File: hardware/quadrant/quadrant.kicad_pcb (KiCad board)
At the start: 4 copper layers, 220 x 200 mm, 347 parts, among them J1 FPC 16, P1 NPTH, Q1 AO3401A, Q111 AO3400A, Q112 AO3401A, Q121 AO3400A, Q122 AO3401A, Q131 AO3400A, Q132 AO3401A, Q141 AO3400A, Q142 AO3401A, Q151 AO3400A, Q152 AO3401A, Q161 AO3400A, Q162 AO3401A, Q171 AO3400A, Q172 AO3401A, Q181 AO3400A, Q182 AO3401A, Q191 AO3400A, Q192 AO3401A, Q2 AO3400A, Q201 AO3400A, Q202 AO3401A, Q211 AO3400A, Q212 AO3401A, Q221 AO3400A, Q222 AO3401A, Q231 AO3400A, Q232 AO3401A, Q241 AO3400A, Q242 AO3401A, Q251 AO3400A, Q252 AO3401A, Q261 AO3400A, Q262 AO3401A, U1 74HC4514, U2 74HC154, U3 ADG1607, U4 ADG1607, U5 AD8421, U6 74LVC1G04, U7 OPA2810, U8 OPA2810

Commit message: Quadrant : build final avec les éventails tenus hors du bord
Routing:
- net M8_B: track 2.21 -> 0.71 mm, vias 1 -> 0
- net M6_B: track 2.21 -> 0.71 mm, vias 1 -> 0
- net M4_B: track 2.21 -> 0.71 mm, vias 1 -> 0
- net M2_B: track 2.21 -> 0.71 mm, vias 1 -> 0
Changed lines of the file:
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@@
   (via (at 14.7 98.65) (size 0.45) (drill 0.2) (layers "F.Cu" "B.Cu") (net 37))
   (segment (start 2.9625 110.075) (end 2.25 110.075) (width 0.2) (layer "F.Cu") (net 117))
-  (segment (start 2.25 110.075) (end 0.75 110.075) (width 0.2) (layer "F.Cu") (net 117))
-  (via (at 0.75 110.075) (size 0.45) (drill 0.2) (layers "F.Cu" "B.Cu") (net 117))
   (segment (start 2.9625 110.575) (end 2.25 110.575) (width 0.2) (layer "F.Cu") (net 112))
   (segment (start 2.25 110.575) (end 1.45 110.575) (width 0.2) (layer "F.Cu") (net 112))
   (via (at 1.45 110.575) (size 0.45) (drill 0.2) (layers "F.Cu" "B.Cu") (net 112))
   (segment (start 2.9625 111.075) (end 2.25 111.075) (width 0.2) (layer "F.Cu") (net 107))
-  (segment (start 2.25 111.075) (end 0.75 111.075) (width 0.2) (layer "F.Cu") (net 107))
-  (via (at 0.75 111.075) (size 0.45) (drill 0.2) (layers "F.Cu" "B.Cu") (net 107))
   (segment (start 2.9625 111.575) (end 2.25 111.575) (width 0.2) (layer "F.Cu") (net 102))
   (segment (start 2.25 111.575) (end 1.45 111.575) (width 0.2) (layer "F.Cu") (net 102))
   (via (at 1.45 111.575) (size 0.45) (drill 0.2) (layers "F.Cu" "B.Cu") (net 102))
   (segment (start 2.9625 112.075) (end 2.25 112.075) (width 0.2) (layer "F.Cu") (net 97))
-  (segment (start 2.25 112.075) (end 0.75 112.075) (width 0.2) (layer "F.Cu") (net 97))
-  (via (at 0.75 112.075) (size 0.45) (drill 0.2) (layers "F.Cu" "B.Cu") (net 97))
   (segment (start 2.9625 112.575) (end 2.25 112.575) (width 0.2) (layer "F.Cu") (net 92))
   (segment (start 2.25 112.575) (end 1.45 112.575) (width 0.2) (layer "F.Cu") (net 92))
   (via (at 1.45 112.575) (size 0.45) (drill 0.2) (layers "F.Cu" "B.Cu") (net 92))
   (segment (start 2.9625 113.075) (end 2.25 113.075) (width 0.2) (layer "F.Cu") (net 87))
-  (segment (start 2.25 113.075) (end 0.75 113.075) (width 0.2) (layer "F.Cu") (net 87))
-  (via (at 0.75 113.075) (size 0.45) (drill 0.2) (layers "F.Cu" "B.Cu") (net 87))
   (segment (start 2.9625 113.575) (end 2.25 113.575) (width 0.2) (layer "F.Cu") (net 82))
   (segment (start 2.25 113.575) (end 1.45 113.575) (width 0.2) (layer "F.Cu") (net 82))

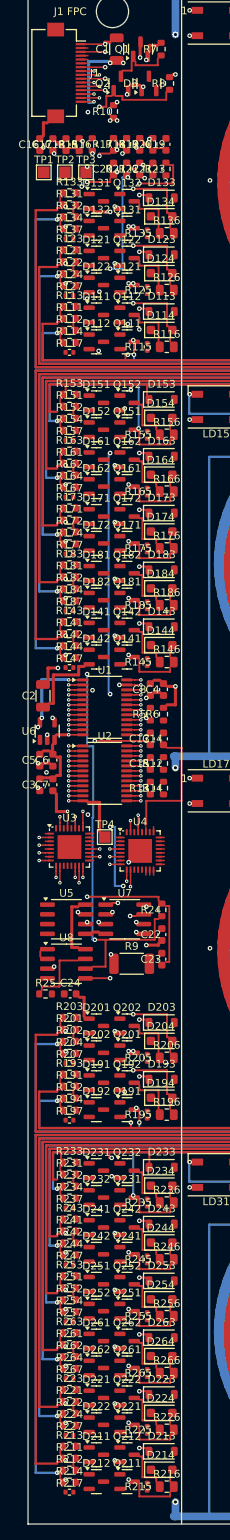
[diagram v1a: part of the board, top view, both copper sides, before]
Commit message: Quadrant 4 x 4 régénéré : schéma dessiné à huit feuilles, roue libre, BAV99W, résultats de build et de DRC
hardware/quadrant : feuille racine et feuilles rails, cells-1 à
cells-4, select, chain, leds ; PCB reroutée avec le nouveau plan de
cellule. Build : aucune route LED ou alimentation ouverte, aucun défaut
d'isolement, neuf nets du frontal à finir dans pcbnew (VREF route
désormais) ; DRC KiCad sans erreur hors éléments non connectés. README
du quadrant et tableau de résultats de la note 14 à jour, avec la ligne
du quadrant 2 x 2.
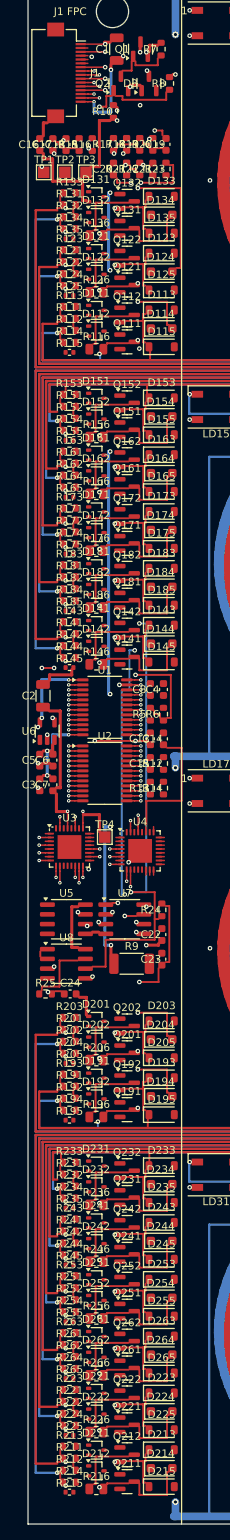
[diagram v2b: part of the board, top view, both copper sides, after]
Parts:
- removed R117, R127, R137, R147, R157, R167, R177, R187, R197, R207, R217, R227, R237, R247, R257, R267: 100k, Resistor_SMD:R_0402_1005Metric
- added D115: B5819W, Diode_SMD:D_SOD-123, F.Cu at (17.4, 46.7)
- added D125: B5819W, Diode_SMD:D_SOD-123, F.Cu at (17.4, 39.3)
- added D135: B5819W, Diode_SMD:D_SOD-123, F.Cu at (17.4, 31.9)
- added D145: B5819W, Diode_SMD:D_SOD-123, F.Cu at (17.4, 87.7)
- added D155: B5819W, Diode_SMD:D_SOD-123, F.Cu at (17.4, 58.1)
- added D165: B5819W, Diode_SMD:D_SOD-123, F.Cu at (17.4, 65.5)
- added D175: B5819W, Diode_SMD:D_SOD-123, F.Cu at (17.4, 72.9)
- added D185: B5819W, Diode_SMD:D_SOD-123, F.Cu at (17.4, 80.3)
- added D195: B5819W, Diode_SMD:D_SOD-123, F.Cu at (17.4, 146.7)
- added D205: B5819W, Diode_SMD:D_SOD-123, F.Cu at (17.4, 139.3)
- added D215: B5819W, Diode_SMD:D_SOD-123, F.Cu at (17.4, 195.1)
- added D225: B5819W, Diode_SMD:D_SOD-123, F.Cu at (17.4, 187.7)
- added D235: B5819W, Diode_SMD:D_SOD-123, F.Cu at (17.4, 158.1)
- added D245: B5819W, Diode_SMD:D_SOD-123, F.Cu at (17.4, 165.5)
- added D255: B5819W, Diode_SMD:D_SOD-123, F.Cu at (17.4, 172.9)
- added D265: B5819W, Diode_SMD:D_SOD-123, F.Cu at (17.4, 180.3)
- D111, D112, D121, D122, D131, D132, D141, D142, D151, D152, D161, D162, D171, D172, D181, D182, D191, D192, D201, D202, D211, D212, D221, D222, D231, D232, D241, D242, D251, D252, D261, D262: value BAV99 -> BAV99W; footprint Package_TO_SOT_SMD:SOT-23 -> Package_TO_SOT_SMD:SOT-323_SC-70
- R7: value 10k -> 470R
- moved R115 10.1 mm to (5.40, 47.4), turned to 0 degrees
- moved R125 10.1 mm to (5.40, 40.0), turned to 0 degrees
- moved R135 10.1 mm to (5.40, 32.6), turned to 0 degrees
- moved R145 10.1 mm to (5.40, 88.4), turned to 0 degrees
- moved R155 10.1 mm to (5.40, 58.8), turned to 0 degrees
- moved R165 10.1 mm to (5.40, 66.2), turned to 0 degrees
- moved R175 10.1 mm to (5.40, 73.6), turned to 0 degrees
- moved R185 10.1 mm to (5.40, 81.0), turned to 0 degrees
- moved R195 10.1 mm to (5.40, 147.4), turned to 0 degrees
- moved R205 10.1 mm to (5.40, 140.0), turned to 0 degrees
- moved R215 10.1 mm to (5.40, 195.8), turned to 0 degrees
- moved R225 10.1 mm to (5.40, 188.4), turned to 0 degrees
- moved R235 10.1 mm to (5.40, 158.8), turned to 0 degrees
- moved R245 10.1 mm to (5.40, 166.2), turned to 0 degrees
- moved R255 10.1 mm to (5.40, 173.6), turned to 0 degrees
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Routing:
- net AMP_OUT: track 0.95 -> 143.1 mm, vias 0 -> 6
- net VREF_DIV: track 41.8 -> 64.4 mm, vias 2 -> 4
- net PULSE_RAIL: track 140.7 -> 124.9 mm, vias 4 -> 8
- net HP_IN: track 101.9 -> 117.1 mm, vias 3 -> 4
- net C2_B: track 674.3 -> 689.0 mm
- net HP_OUT: track 116.1 -> 104.1 mm, vias 6 -> 2
- net GND: track 2287.2 -> 2276.9 mm, vias 82 -> 81
- net 5VA: track 221.5 -> 212.8 mm, vias 8 -> 4
- net LP_OUT: track 115.3 -> 122.4 mm, vias 8 -> 5
- net OUT_FB: track 131.8 -> 124.7 mm
- net LP_IN: track 119.3 -> 112.6 mm, vias 7 -> 3
- net C3_B: track 733.5 -> 727.3 mm, vias 5 -> 3
- net VREF: track 208.6 -> 214.0 mm
- net LP_FB: track 104.8 -> 101.8 mm, vias 3 -> 2
- net C13_A: track 1587.2 -> 1590.2 mm, vias 5 -> 3
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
